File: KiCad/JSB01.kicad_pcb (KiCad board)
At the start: 2 copper layers, 88 x 33 mm, 35 parts, among them J1 MB10XX Sonar, J2 VL53LXX TOF(0x29), M1 LD14, Q2 AO3400A, SW1 Tactile, SW2 Tactile, SW3 Slide, U1 TPS61291DRVR, U2 QMC5883L(0x0D), U3 BH1750FVI(0x23)

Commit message: BTO ver. (QMC5883P)
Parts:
- removed C3: 0.22uF, Capacitor_SMD:C_0603_1608Metric
- removed MCU1: XIAO RP2040, JSB01_Lib:MOUDLE14P-2.54-21X17.8MM
- removed the Pad at (41.9, 39.9)
- removed the Pad at (44.5, 35.4)
- removed the Pad at (40.0, 39.9)
- removed the Pad at (44.5, 39.9)
- removed the Pad at (41.9, 35.4)
- removed the Pad at (40.0, 35.4)
- removed the REF** at (27.4, 65.3)
- removed the REF** at (111.4, 65.3)
- removed the REF** at (27.4, 36.3)
- removed the REF** at (111.4, 36.3)
- added ?: , , F.Cu at (83.3, 48.8)
- added C10: 33p, Capacitor_SMD:C_0603_1608Metric, F.Cu at (52.5, 41.1)
- added C11: 100n, Capacitor_SMD:C_0402_1005Metric, F.Cu at (41.3, 46.4)
- added C12: 100n, Capacitor_SMD:C_0402_1005Metric, F.Cu at (46.5, 46.4)
- added C13: 100n, Capacitor_SMD:C_0402_1005Metric, F.Cu at (37.0, 40.9)
- added C14: 100n, Capacitor_SMD:C_0402_1005Metric, F.Cu at (49.5, 41.1)
- added C15: 100n, Capacitor_SMD:C_0402_1005Metric, F.Cu at (49.5, 40.0)
- added C16: 100n, Capacitor_SMD:C_0402_1005Metric, F.Cu at (38.9, 40.9)
- added C17: 100n, Capacitor_SMD:C_0402_1005Metric, F.Cu at (38.9, 38.1)
- added C18: 100n, Capacitor_SMD:C_0402_1005Metric, F.Cu at (38.9, 37.2)
- added C19: 100n, Capacitor_SMD:C_0402_1005Metric, F.Cu at (41.3, 36.2)
- added C20: 100n, Capacitor_SMD:C_0402_1005Metric, F.Cu at (45.5, 36.2)
- added C21: 100u, JSB01_Lib:CAP-SMD_L6.0-W3.2, F.Cu at (54.4, 50.5)
- added C7: 10u, Capacitor_SMD:C_0603_1608Metric, F.Cu at (27.5, 30.3)
- added C8: 10u, Capacitor_SMD:C_0603_1608Metric, F.Cu at (27.5, 28.4)
- added C9: 33p, Capacitor_SMD:C_0603_1608Metric, F.Cu at (52.5, 46.2)
- added D1: LED, JSB01_Lib:LED0603-RD_GREEN, F.Cu at (50.2, 37.1)
- added D2: NSR0320MW2T1G, JSB01_Lib:SOD-323_L1.8-W1.3-LS2.5-RD, F.Cu at (27.5, 32.2)
- added D3: 1N5819WS, JSB01_Lib:SOD-323_L1.8-W1.3-LS2.5-RD, F.Cu at (36.9, 25.4)
- added JP2: SolderJumper_2_Open, Jumper:SolderJumper-2_P1.3mm_Open_RoundedPad1.0x1.5mm, F.Cu at (77.0, 48.1)
- added JP3: SolderJumper_2_Open, JSB01_Lib:SolderJumper-2_Open_mini, F.Cu at (53.6, 35.5)
- added Pad: Pad1.2_0.8, JSB01_Lib:Pad1.2_0.8, F.Cu at (71.1, 38.1)
- added Pad: Pad0.6_0.35, JSB01_Lib:Pad0.6_0.35, F.Cu at (62.5, 36.6)
- added Pad: Pad0.6_0.35, JSB01_Lib:Pad0.6_0.35, F.Cu at (70.6, 36.6)
- added Pad: Pad1.2_0.8, JSB01_Lib:Pad1.2_0.8, F.Cu at (63.0, 38.1)
- added R10: 27.4, Resistor_SMD:R_0402_1005Metric, F.Cu at (38.9, 40.0)
- added R11: 27.4, Resistor_SMD:R_0402_1005Metric, F.Cu at (38.9, 39.1)
- added R12: 470, Resistor_SMD:R_0603_1608Metric, F.Cu at (47.6, 36.3)
- added R13: 470K, Resistor_SMD:R_0603_1608Metric, F.Cu at (64.0, 49.1)
- added R14: 390K, Resistor_SMD:R_0603_1608Metric, F.Cu at (64.0, 46.0)
- added R15: 1M, Resistor_SMD:R_0603_1608Metric, F.Cu at (58.3, 44.9)
- added R3: 5.1K, Resistor_SMD:R_0402_1005Metric, F.Cu at (34.1, 40.6)
- added R4: 5.1K, Resistor_SMD:R_0402_1005Metric, F.Cu at (34.1, 35.6)
- added R8: 1K, Resistor_SMD:R_0603_1608Metric, F.Cu at (52.5, 39.5)
- added R9: 1k, Resistor_SMD:R_0603_1608Metric, F.Cu at (31.8, 51.2)
- added REF**: MountingHole_2.2mm_M2, MountingHole:MountingHole_2.2mm_M2, F.Cu at (27.4, 25.1)
- added REF**: MountingHole_2.2mm_M2, MountingHole:MountingHole_2.2mm_M2, F.Cu at (27.4, 51.1)
- added SW4: SKRPABE010, JSB01_Lib:KEY-SMD_4P-L4.2-W3.2, F.Cu at (32.0, 46.2)
- added SW5: SKRPABE010, JSB01_Lib:KEY-SMD_4P-L4.2-W3.2, F.Cu at (27.9, 46.2)
- added U3: TPS61025DRCR, JSB01_Lib:VSON-10_L3.0-W3.0-P0.50-BL-EP, F.Cu at (60.6, 47.6)
- added U4: AMS1117-3.3, JSB01_Lib:SOT-223-3_L6.5-W3.4, F.Cu at (32.6, 27.6)
- added U5: QMC5883P(0x2C), JSB01_Lib:LGA-16_L3.0-W3.0-P0.50-BL_SQ, F.Cu at (79.8, 26.0)
- added Y1: TAXM12M4RLBDDT2T, JSB01_Lib:OSC-SMD_4P-L3.2-W2.5, F.Cu at (52.5, 43.6)
- BT1: value 2xAAA -> 1xAAA; footprint JSB01_Lib:BatteryHolder 2xAAA -> JSB01_Lib:BatteryHolder_SN4_1PC
- C1: value 10uF -> 10u
- C2: value 22uF -> 2.2u
- C4: value 0.1uF -> 0.1u
- C5: value 4.7uF -> 4.7u
- C6: value 1uF -> 1u
- J2: value VL53LXX TOF(0x29) -> USB_C_Receptacle_USB2.0; footprint Connector_PinSocket_2.54mm:PinSocket_1x06_P2.54mm_Vertical -> JSB01_Lib:USB-C-SMD_TYPE-C-16P-1; moved to F.Cu
- L1: value 3.3μH -> 6.8μH
- R1, R2: value 10KΩ -> 4.7K
- R5: value 100KΩ -> 100K
- R6: value 20KΩ -> 20K
- SW1, SW2: footprint JSB01_Lib:SW_tactile_DTS6 -> JSB01_Lib:SW-SMD_4P-L4.5-W4.5-P3.00-LS6.8
- U1: value TPS61291DRVR -> RP2040; footprint JSB01_Lib:WSON-6_L2.0-W2.0-P0.65-BL-EP -> JSB01_Lib:RP2040-QFN-56
- U2: value QMC5883L(0x0D) -> W25Q128JVSIQ; footprint JSB01_Lib:LGA-16_L3.0-W3.0-P0.50-BL_SQ -> JSB01_Lib:SOP-8-208mil
- moved J2 79.9 mm to (30.2, 38.1), turned to -90 degrees
- moved U2 68.6 mm to (36.8, 47.6), turned to 0 degrees
- moved U1 43.0 mm to (44.5, 41.3), turned to 90 degrees
- moved JP1 36.8 mm to (69.3, 46.3)
- moved J1 32.5 mm to (74.9, 37.7)
- moved R1 32.1 mm to (71.9, 26.2)
- moved R7 31.0 mm to (83.0, 25.6), turned to -90 degrees
- moved U6 30.3 mm to (86.0, 25.6)
- moved R2 28.0 mm to (70.0, 26.2)
- moved C4 27.9 mm to (76.0, 25.0)
- moved C5 27.9 mm to (76.0, 26.9)
- moved C6 27.1 mm to (84.7, 29.0)
- moved SW1 26.3 mm to (70.9, 38.1), turned to 90 degrees
- moved C1 25.8 mm to (62.0, 50.7)
- moved SW3 23.9 mm to (79.4, 49.8)
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- renumbered U3 to U6
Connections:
- C2 pad 1: +3.3V -> +3V3
- C4 pad 1: +3.3V -> +3V3
- C5 pad 1: Net-(U2-C1) -> Net-(U5-C1)
- J1 pad 2: +3.3V -> +3V3
- J1 pad 6: Net-(J1-PW) -> SONAR_PW
- L1 pad 2: Net-(U1-SW) -> Net-(U3-SW)
- M1 pad 1: +3.3V -> +3V3
- R1 pad 1: +3.3V -> +3V3
- R1 pad 2: Net-(J2-SDA) -> SDA
- R2 pad 1: +3.3V -> +3V3
- R2 pad 2: Net-(J2-SCL) -> SCL
- R6 pad 1: Net-(MCU1-D2) -> VIB
- R7 pad 1: +3.3V -> +3V3
- SW1 pad 1: Net-(MCU1-D0) -> SW1
- SW1 pad 2: GND -> SW1
- SW2 pad 1: Net-(MCU1-D1) -> SW2
- SW2 pad 2: GND -> SW2
- U1 pad 1: Net-(U1-SW) -> +3V3
- U1 pad 2: +3.3V -> SW1
- U1 pad 3: Net-(JP1-A) -> SW2
- U1 pad 4: Net-(JP1-A) -> VIB
- U1 pad 5: GND -> unconnected-(U1-GPIO3-Pad5)
- U1 pad 6: GND -> SDA
- U1 pad 7: GND -> SCL
- U2 pad 1: Net-(J2-SCL) -> QSPI_SS
- U2 pad 2: +3.3V -> QSPI_SD1
- U2 pad 3: unconnected-(U2-Pad3) -> QSPI_SD2
- U2 pad 4: +3.3V -> GND
- U2 pad 5: unconnected-(U2-Pad5) -> QSPI_SD0
- U2 pad 6: unconnected-(U2-Pad6) -> QSPI_SCLK
- U2 pad 7: unconnected-(U2-Pad7) -> QSPI_SD3
- U2 pad 8: Net-(U2-SETP) -> +3V3
- U6 pad 1: +3.3V -> +3V3
- U6 pad 4: Net-(J2-SDA) -> SDA
- U6 pad 6: Net-(J2-SCL) -> SCL
- U6 pad 7: unconnected-(U3-EP-Pad7) -> GND
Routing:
- net +3.3V: track 228.7 -> 0.00 mm
- net +3V3: track 0.00 -> 177.1 mm, vias 0 -> 6
- net Net-(J2-SDA): track 93.8 -> 0.00 mm, vias 2 -> 0
- net Net-(J2-SCL): track 89.9 -> 0.00 mm, vias 2 -> 0
- net Net-(MCU1-D0): track 66.7 -> 0.00 mm, vias 1 -> 0
- net SCL: track 0.00 -> 66.3 mm, vias 0 -> 6
- net SDA: track 0.00 -> 64.5 mm, vias 0 -> 4
- net Net-(J1-PW): track 62.5 -> 0.00 mm
- net GND: track 198.1 -> 253.9 mm, vias 15 -> 18
- net Net-(MCU1-D1): track 49.9 -> 0.00 mm, vias 1 -> 0
- net SONAR_PW: track 0.00 -> 43.2 mm, vias 0 -> 1
- net SW1: track 0.00 -> 38.4 mm, vias 0 -> 1
- net RESET: track 0.00 -> 31.8 mm, vias 0 -> 2
- net SW2: track 0.00 -> 29.5 mm, vias 0 -> 1
- net Net-(JP1-A): track 29.0 -> 56.6 mm
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- added copper zone on F.Cu, net +3V3
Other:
- board size 88 x 33 mm -> 62 x 30 mm
- board text added: "JSB01 Rev 1.0"
- board text removed: "JSB01 Rev 0.1"

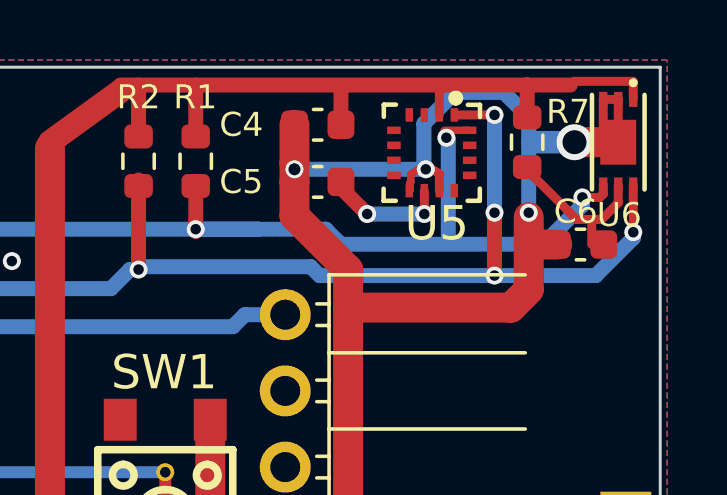
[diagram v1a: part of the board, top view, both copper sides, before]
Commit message: BH1750FVI move to left
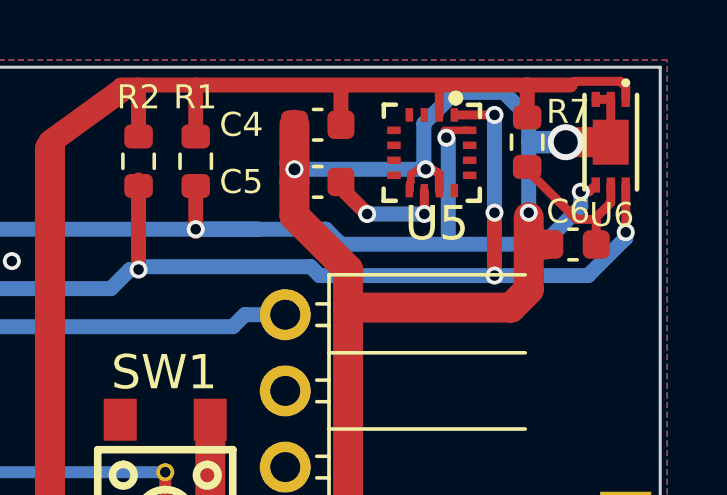
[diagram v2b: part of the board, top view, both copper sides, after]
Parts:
- moved C6 0.25 mm to (84.5, 29.0)
- moved U6 0.25 mm to (85.8, 25.6)
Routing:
- net GND: track 253.9 -> 252.5 mm
- net Net-(U6-DVI): track 5.70 -> 5.18 mm
